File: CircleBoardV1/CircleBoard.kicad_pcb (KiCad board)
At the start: 2 copper layers, 264 x 264 mm, 107 parts, among them J1 USB4125-GF-A-0190, P1 LEDS4

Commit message: Front decorated
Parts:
- removed XD1, XD2: MountingHole_3.2mm_M3_DIN965_Pad, MountingHole:MountingHole_3.2mm_M3_DIN965_Pad
- added J1: USB4125-GF-A-0190, SamacSys_Parts:USB4125GFA0190, F.Cu at (129.1, 254.6)
- moved J1 2.67 mm to (127.6, -4.40)
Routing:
- net LINK102: track 0.00 -> 32.1 mm
- net GND: track 9.50 -> 12.1 mm, vias 104 -> 106
- net LINK00: track 49.3 -> 48.4 mm
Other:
- board text added: "GND D 5V"
- board text added: "IN"
- board text added: "OUT"
- board text added: "enjoy :)"
- board text added: "kylarLEDs"

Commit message: All LEDs are connected... not to controller yet
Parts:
- added U2: Pico, MCU_RaspberryPi_and_Boards:RPi_Pico_SMD_TH_removes_novia, F.Cu at (127.6, 125.1)
- added led45: LED_WS2812B_PLCC4_5.0x5.0mm_P3.2mm, LED_WS2812B_PLCC4_5.0x5.0mm_P3.2mm, F.Cu at (107.8, 116.5)
- added led45: LED_WS2812B_PLCC4_5.0x5.0mm_P3.2mm, LED_WS2812B_PLCC4_5.0x5.0mm_P3.2mm, F.Cu at (147.9, 137.2)
- added led45: LED_WS2812B_PLCC4_5.0x5.0mm_P3.2mm, LED_WS2812B_PLCC4_5.0x5.0mm_P3.2mm, F.Cu at (147.9, 116.5)
- added led45: LED_WS2812B_PLCC4_5.0x5.0mm_P3.2mm, LED_WS2812B_PLCC4_5.0x5.0mm_P3.2mm, F.Cu at (107.8, 137.2)
- moved led45 18.1 mm to (107.8, 105.3)
- moved led60 16.5 mm to (147.9, 147.8)
- moved led44 14.5 mm to (147.9, 105.3)
- moved led53 12.9 mm to (107.8, 147.8)
- moved led54 7.11 mm to (147.9, 126.8)
- moved led46 5.99 mm to (107.8, 126.8)
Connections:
- led44 pad 2: LINK45 -> link_45_a
- led45 pad 2: LINK46 -> LINK47
- led45 pad 4: LINK45 -> link_45_b
- led46 pad 2: LINK47 -> link_47_b
- led46 pad 4: LINK46 -> link_46_b
- led52 pad 2: LINK53 -> LINK61
- led53 pad 2: LINK54 -> link_54_b
- led53 pad 4: LINK53 -> link_53_a
- led54 pad 2: LINK55 -> link_55_a
- led54 pad 4: LINK54 -> link_54_a
- led55 pad 4: LINK55 -> link_61_a
- led59 pad 2: LINK60 -> link_53_a
- led60 pad 2: LINK61 -> link_61_a
- led60 pad 4: LINK60 -> link_60_a
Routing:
- net link_53_a: track 0.00 -> 77.9 mm, vias 0 -> 2
- net LINK60: track 56.0 -> 0.00 mm, vias 2 -> 0
- net LINK61: track 65.3 -> 16.8 mm, vias 2 -> 0
- net LINK53: track 37.4 -> 0.00 mm
- net LINK54: track 34.5 -> 0.00 mm
- net link_61_a: track 0.00 -> 33.8 mm
- net LINK55: track 33.2 -> 0.00 mm
- net LINK102: track 32.1 -> 0.00 mm
- net link_45_b: track 0.00 -> 16.4 mm
- net link_54_b: track 0.00 -> 15.8 mm
- net link_46_b: track 0.00 -> 15.6 mm
- net link_47_b: track 0.00 -> 15.5 mm
- net LINK45: track 14.5 -> 1.67 mm
- net LINK46: track 12.2 -> 0.00 mm
- net link_45_a: track 0.00 -> 9.93 mm
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
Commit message: before clean
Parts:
- removed H1: PinHeader_1x03_P2.54mm_Vertical, Connector_PinHeader_2.54mm:PinHeader_1x03_P2.54mm_Vertical
- removed P1: LEDS4, SamacSys_Parts:LEDS4_copy
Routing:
- net LINK00: track 47.4 -> 33.1 mm
- net LINK11: track 81.6 -> 77.7 mm
- net LINK27: track 19.7 -> 16.6 mm
- net LINK24: track 66.7 -> 64.1 mm
- net LINK39: track 70.1 -> 68.1 mm
- net LINK22: track 64.2 -> 63.1 mm
- net GND: vias 112 -> 111

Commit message: ready for enc and mic
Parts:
- added LEDS0: ledstrip_3pin_10mm, kylarLEDs:ledstrip_3pin_10mm, F.Cu at (123.6, 128.3)
- added LEDS1: ledstrip_3pin_10mm, kylarLEDs:ledstrip_3pin_10mm, F.Cu at (131.0, 128.3)
- added LEDS2: ledstrip_3pin_10mm, kylarLEDs:ledstrip_3pin_10mm, F.Cu at (123.8, 143.6)
- added LEDS3: ledstrip_3pin_10mm, kylarLEDs:ledstrip_3pin_10mm, F.Cu at (131.1, 143.6)
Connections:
- J1 pad A5: LINK00 -> (no net)
- J1 pad B5: LINK00 -> (no net)
- J1 pad A5: LINK102 -> (no net)
- J1 pad B5: LINK102 -> (no net)
- U2 pad GP14: (no net) -> LEDS0
- U2 pad GP15: (no net) -> LEDS1
- U2 pad GP16: (no net) -> LEDS3
- U2 pad GP17: (no net) -> LEDS2
- led0 pad 4: LINK00 -> LEDS0
- led101 pad 2: LINK102 -> (no net)
- led25 pad 4: LINK25 -> LEDS1
- led55 pad 2: LINK56 -> (no net)
- led56 pad 4: LINK56 -> LEDS2
- led70 pad 2: LINK71 -> (no net)
- led71 pad 4: LINK71 -> LEDS3
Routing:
- net LEDS0: track 0.00 -> 185.4 mm, vias 0 -> 2
- net LEDS1: track 0.00 -> 167.0 mm, vias 0 -> 2
- net LEDS3: track 0.00 -> 107.1 mm, vias 0 -> 2
- net LEDS2: track 0.00 -> 98.4 mm, vias 0 -> 4
- net LINK25: track 61.8 -> 0.00 mm
- net LINK56: track 44.5 -> 0.00 mm
- net LINK71: track 35.0 -> 0.00 mm
- net LINK00: track 33.1 -> 0.00 mm
- net LINK26: track 30.5 -> 22.1 mm, vias 0 -> 2
- net GND: track 11.9 -> 5.96 mm, vias 111 -> 112
- net LINK45: track 1.67 -> 0.00 mm
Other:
- board text added: "-0"
- board text added: "-1"
- board text added: "-2"
- board text added: "-3"
- board text added: "G .... 5V"
- board text added: "LEDS-0"
- board text added: "LEDS-1"
- board text added: "LEDS-2"
- board text added: "LEDS-3"
- board text added: "LEDS0,1,2=25 leds LEDS3=31 leds"
- board text removed: "5V"
- board text removed: "D"
- board text removed: "GND"

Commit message: moved edge cut to center better
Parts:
- moved J1 2.08 mm to (127.2, 255.4)
- moved J1 1.66 mm to (128.5, -3.00)
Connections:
- J1 pad MH3: (no net) -> GND
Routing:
- net GND: track 5.96 -> 21.6 mm
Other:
- board text removed: "IN"
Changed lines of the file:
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@@
   )
   (footprint "SamacSys_Parts:USB4125GFA0190" locked (layer "F.Cu")
-    (at 127.6 -4.4 180)
+    (at 128.5 -3 180)
     (descr "USB4125-GF-A-0190-2")
     (tags "Connector")
@@
   )
   (footprint "SamacSys_Parts:USB4125GFA0190" (layer "F.Cu")
-    (at 129.1 254.6)
+    (at 127.18 255.4)
     (descr "USB4125-GF-A-0190-2")
     (tags "Connector")
@@
       (net 1 "GND") (pinfunction "MH2") (pintype "passive"))
     (pad "MH3" thru_hole circle locked (at 4.32 0.8) (size 2.01 2.01) (drill 1.34) (layers *.Cu *.Mask)
-      (pinfunction "MH3") (pintype "passive"))
+      (net 1 "GND") (pinfunction "MH3") (pintype "passive"))
     (pad "MH4" thru_hole circle locked (at 4.32 -3) (size 2.01 2.01) (drill 1.34) (layers *.Cu *.Mask)
       (net 1 "GND") (pinfunction "MH4") (pintype "passive"))
@@
   (gr_circle (center 69.7 125.6) (end 87.4 115.7) (layer "F.SilkS") (width 0.15) (fill none))
   (gr_circle (center 97.6 175.3) (end 115.1 181.9) (layer "F.SilkS") (width 0.15) (fill none))
-  (gr_circle (center 127.5 125) (end 259.5 125) (layer "Edge.Cuts") (width 0.1) (fill none))
+  (gr_circle (center 127.9 126.4) (end 259.9 126.4) (layer "Edge.Cuts") (width 0.1) (fill none))
   (gr_text "GND D 5V" (at 139.3 4.2) (layer "B.SilkS")
     (effects (font (size 1 1) (thickness 0.15)) (justify mirror))
@@
     (effects (font (size 1 1) (thickness 0.15)) (justify mirror))
   )
-  (gr_text "IN" (at 117.3 -0.6) (layer "F.SilkS")
-    (effects (font (size 6 6) (thickness 0.6)))
-  )
   (gr_text "-3" (at 160.7 242.6) (layer "F.SilkS")
     (effects (font (size 1.5 1.5) (thickness 0.3)))
@@
     (effects (font (size 2 2) (thickness 0.2)))
   )
-  (segment (start 130.35 -1.32) (end 131.84 -1.32) (width 0.5) (layer "F.Cu") (net 1))
-  (segment (start 126.35 251.52) (end 124.86 251.52) (width 0.5) (layer "F.Cu") (net 1))
-  (segment (start 124.85 -1.32) (end 123.36 -1.32) (width 0.5) (layer "F.Cu") (net 1))
-  (segment (start 131.85 251.52) (end 133.34 251.52) (width 0.5) (layer "F.Cu") (net 1))
+  (segment (start 132.74 0.08) (end 132.82 0) (width 0.5) (layer "F.Cu") (net 1))
+  (segment (start 122.94 252.32) (end 122.86 252.4) (width 0.5) (layer "F.Cu") (net 1))
+  (segment (start 131.42 252.32) (end 131.5 252.4) (width 0.5) (layer "F.Cu") (net 1))
+  (segment (start 125.75 0.08) (end 124.26 0.08) (width 0.5) (layer "F.Cu") (net 1))
+  (segment (start 131.25 0.08) (end 132.74 0.08) (width 0.5) (layer "F.Cu") (net 1))
+  (segment (start 129.93 252.32) (end 131.42 252.32) (width 0.5) (layer "F.Cu") (net 1))
+  (segment (start 124.43 252.32) (end 122.94 252.32) (width 0.5) (layer "F.Cu") (net 1))
+  (segment (start 124.26 0.08) (end 124.18 0) (width 0.5) (layer "F.Cu") (net 1))
   (via (at 110.2 138.8) (size 0.6) (drill 0.3) (layers "F.Cu" "B.Cu") (net 1))
   (via (at 84.315 173.939) (size 0.6) (drill 0.3) (layers "F.Cu" "B.Cu") (net 1))
@@
   (via (at 97.142 250.012) (size 0.6) (drill 0.3) (layers "F.Cu" "B.Cu") (net 1))
   (via (at 175.247 173.939) (size 0.6) (drill 0.3) (layers "F.Cu" "B.Cu") (net 1))
+  (segment (start 132.82 -3.8) (end 132.82 0) (width 0.5) (layer "B.Cu") (net 1))
+  (segment (start 122.86 256.2) (end 122.86 252.4) (width 0.5) (layer "B.Cu") (net 1))
+  (segment (start 131.5 256.2) (end 131.5 252.4) (width 0.5) (layer "B.Cu") (net 1))
+  (segment (start 124.18 -3.8) (end 124.18 0) (width 0.5) (layer "B.Cu") (net 1))
   (segment (start 140.8016 13.8557) (end 150.2265 13.8557) (width 0.25) (layer "F.Cu") (net 3))
   (segment (start 160.5057 3.5765) (end 160.5057 2.464) (width 0.25) (layer "F.Cu") (net 3))

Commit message: mic and enc almost done
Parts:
- added C1: C0603, easyeda:C0603, F.Cu at (156.8, 124.1)
- added C2: C0603, easyeda:C0603, F.Cu at (156.9, 130.8)
- added C3: C0603, easyeda:C0603, F.Cu at (215.0, 131.0)
- added C4: C0603, easyeda:C0603, F.Cu at (215.0, 125.0)
- added ENC1: PEC12R-4215F-S0024, SamacSys_Parts:PEC12R-4XXXF-SXXXX_court, F.Cu at (228.3, 127.9)
- added MIC_0: MIC-SMD_8P-L3.0-W4.0-P0.85-BL, easyeda:MIC-SMD_8P-L3.0-W4.0-P0.85-BL, F.Cu at (161.6, 124.3)
- added MIC_1: MIC-SMD_4P-L3.8-W2.3-P2.66-BR, easyeda:MIC-SMD_4P-L3.8-W2.3-P2.66-BR, F.Cu at (161.5, 130.8)
- added R1: R0603, easyeda:R0603, F.Cu at (211.1, 131.0)
- added R1: R0603, easyeda:R0603, F.Cu at (211.2, 125.0)
- renumbered J1 to USB1
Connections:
- U2 pad 18: (no net) -> GND
- U2 pad 29: (no net) -> ENC_SW
- U2 pad 34: (no net) -> ADC2
- U2 pad 36: (no net) -> 3V3
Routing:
- net ENC_A_raw: track 0.00 -> 10.3 mm
- net ENC_B_raw: track 0.00 -> 9.75 mm
- net LINK74: track 60.5 -> 65.7 mm
- net GND: vias 112 -> 114

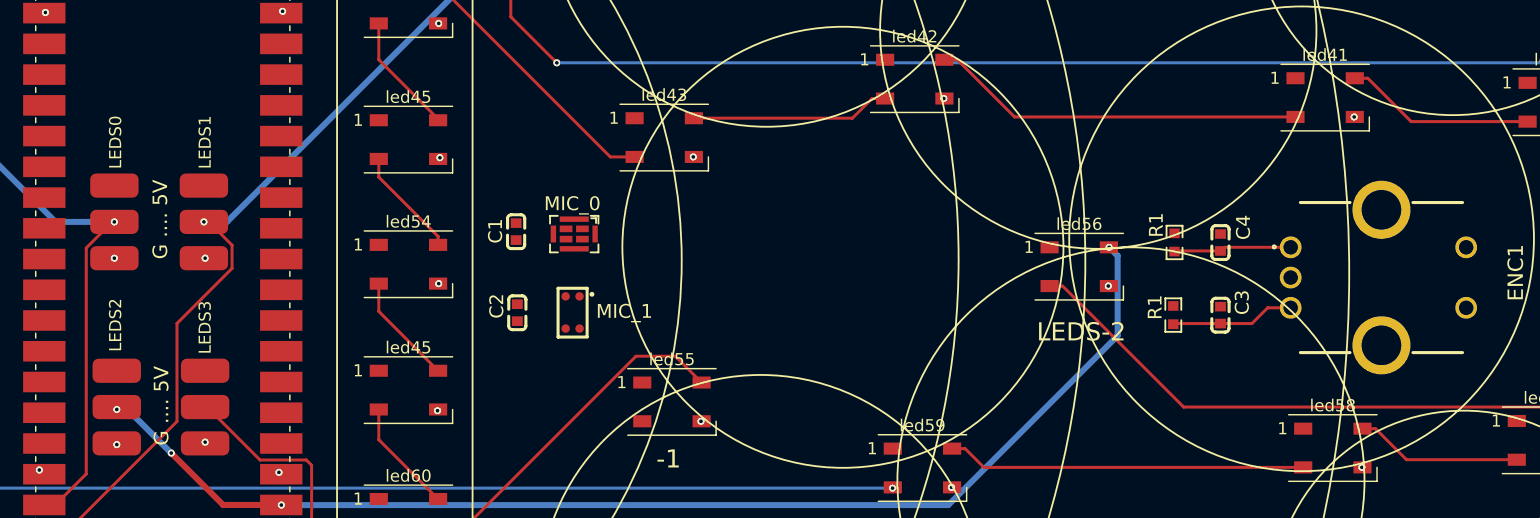
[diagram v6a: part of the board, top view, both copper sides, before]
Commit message: Mic and Enc ready
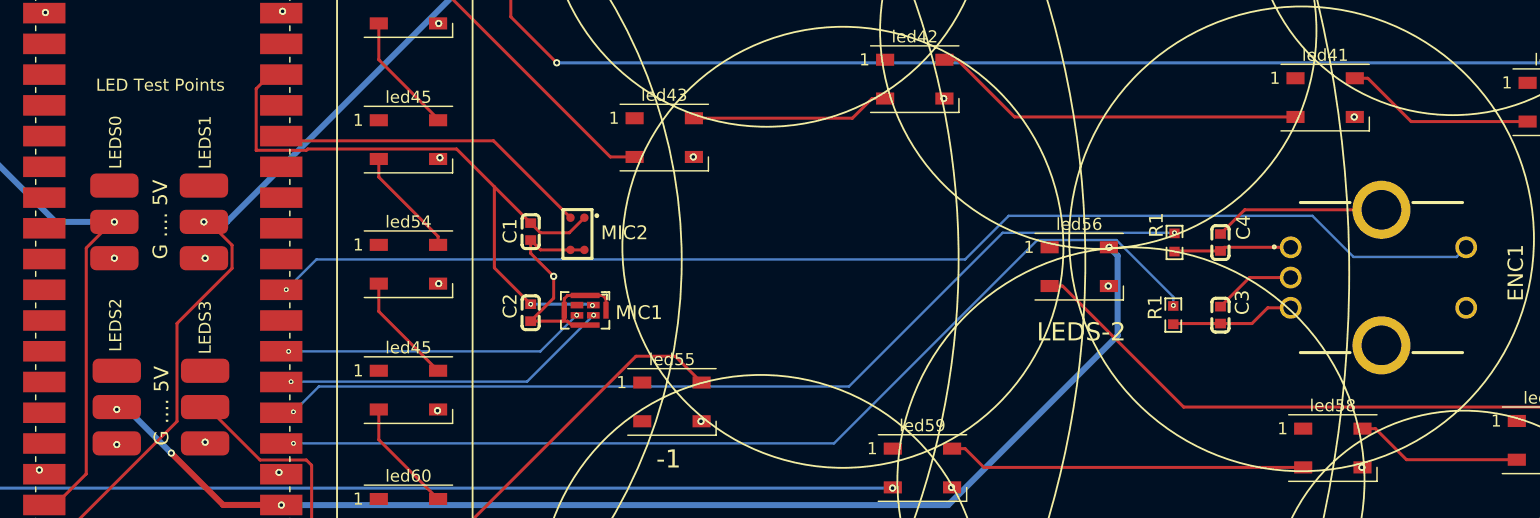
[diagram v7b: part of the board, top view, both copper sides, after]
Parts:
- moved MIC2 6.51 mm to (161.9, 124.3)
- moved MIC1 6.36 mm to (162.5, 130.6)
- moved C1 1.20 mm to (158.0, 124.1)
- moved C2 1.10 mm to (158.0, 130.8)
- renumbered MIC_0 to MIC1, MIC_1 to MIC2
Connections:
- ENC1 pad 4: GND -> ENC_SW
- ENC1 pad 5: ENC_SW -> GND
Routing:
- net ENC_SW: track 0.00 -> 101.8 mm, vias 0 -> 1
- net ENC_A: track 0.00 -> 82.3 mm, vias 0 -> 2
- net ENC_B: track 0.00 -> 78.9 mm, vias 0 -> 2
- net 3V3: track 0.00 -> 53.4 mm, vias 0 -> 2
- net GND: track 21.6 -> 66.8 mm, vias 114 -> 115
- net ADC2: track 0.00 -> 27.6 mm
- net PDM_DATA: track 0.00 -> 27.3 mm, vias 0 -> 2
- net PDM_CLK: track 0.00 -> 25.0 mm, vias 0 -> 2
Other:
- board text added: "LED Test Points"
